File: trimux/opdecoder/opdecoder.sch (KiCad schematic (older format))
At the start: 28 parts, among them J1 Conn_01x05, J11 Conn_01x05, J2 Conn_01x01, J3 Conn_01x01, J4 Conn_01x05, J5 Conn_01x01, J6 Conn_01x01, J7 Conn_01x01, J8 Conn_01x05, P1 CONN_01X03, P2 CONN_01X03, P3 CONN_01X03, U1 trimux, U10 trimux, U2 trimux, U3 trimux, U4 trimux, U5 trimux, U7 trimux, U8 trimux, U9 trimux

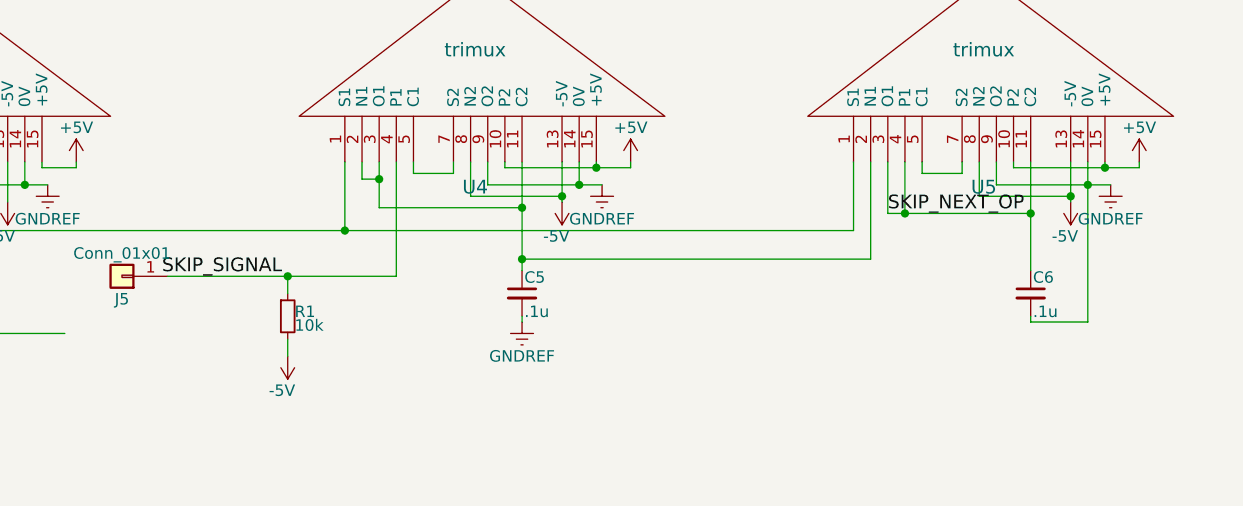
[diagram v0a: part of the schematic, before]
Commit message: opcode decoder
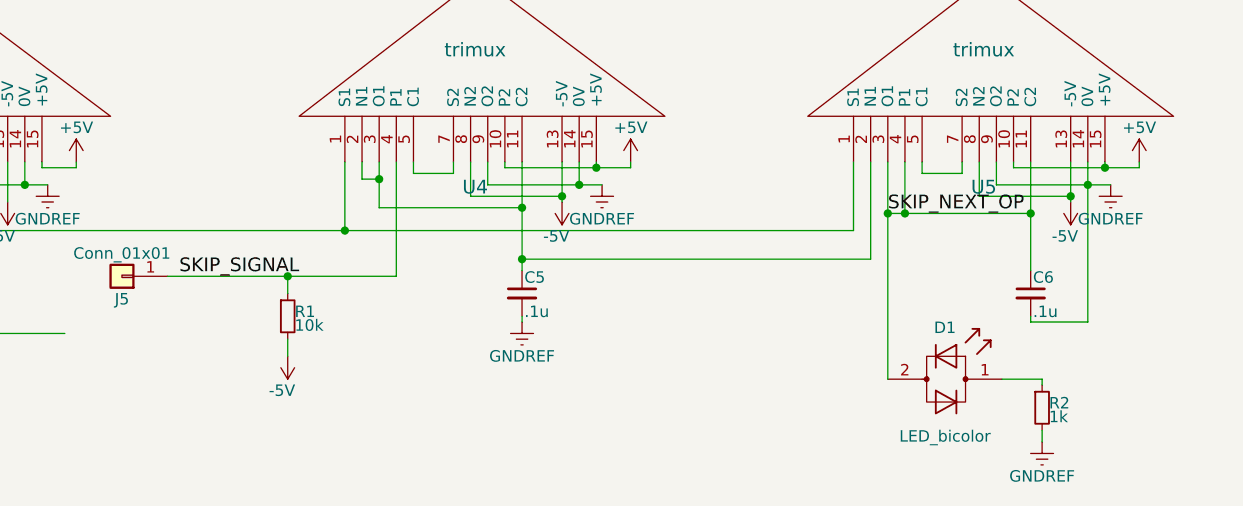
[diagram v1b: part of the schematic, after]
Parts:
- added D1: LED_bicolor, LEDs:LED_D5.0mm, symbol LED_bicolor
- added R2: 1k, Resistors_SMD:R_1206_HandSoldering, symbol R_Small
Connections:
- wire segments 257 -> 260
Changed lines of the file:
@@
 	1    0    0    -1
 $EndComp
-Text Label 3825 5650 0    60   ~ 0
+Text Label 3900 5650 0    60   ~ 0
 SKIP_SIGNAL
 Text Label 1675 5450 0    60   ~ 0
@@
 Connection ~ 7625 5375
 Wire Wire Line
-	7000 5375 7000 5150
+	7000 5150 7000 6100
 Connection ~ 7075 5375
 Wire Wire Line
@@
 	1625 5700 1500 5700
 Connection ~ 1625 5450
+$Comp
+L LED_bicolor D1
+U 1 1 5A2348D1
+P 7250 6100
+F 0 "D1" H 7250 6325 50  0000 C CNN
+F 1 "LED_bicolor" H 7250 5850 50  0000 C CNN
+F 2 "LEDs:LED_D5.0mm" H 7250 6100 50  0001 C CNN
+F 3 "" H 7250 6100 50  0001 C CNN
+	1    7250 6100
+	1    0    0    -1
+$EndComp
+$Comp
+L R_Small R2
+U 1 1 5A234CCC
+P 7675 6225
+F 0 "R2" H 7705 6245 50  0000 L CNN
+F 1 "1k" H 7705 6185 50  0000 L CNN
+F 2 "Resistors_SMD:R_1206_HandSoldering" H 7675 6225 50  0001 C CNN
+F 3 "" H 7675 6225 50  0001 C CNN
+	1    7675 6225
+	1    0    0    -1
+$EndComp
+Wire Wire Line
+	7500 6100 7675 6100
+Wire Wire Line
+	7675 6100 7675 6125
+Connection ~ 7000 5375
+Wire Wire Line
+	7675 6325 7675 6375
+$Comp
+L GNDREF #PWR036
+U 1 1 5A235831
+P 7675 6375
+F 0 "#PWR036" H 7675 6125 50  0001 C CNN
+F 1 "GNDREF" H 7675 6225 50  0000 C CNN
+F 2 "" H 7675 6375 50  0000 C CNN
+F 3 "" H 7675 6375 50  0000 C CNN
+	1    7675 6375
+	1    0    0    -1
+$EndComp
 $EndSCHEMATC
